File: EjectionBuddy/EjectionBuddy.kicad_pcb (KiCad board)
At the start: 4 copper layers, 48 x 53.5 mm, 117 parts, among them J10 Conn_01x04, J11 Conn_01x02, J12 Conn_01x04, J13 Conn_01x04, J14 Conn_01x08, J15 USB_C_Receptacle_USB2.0_14P, J2 Conn_01x04, J3 Conn_01x04, J4 Conn_01x04, J5 Conn_01x04, J6 Conn_01x08, J7 Conn_01x04, J8 Conn_01x04, J9 Conn_01x04, Q1 NCE55P04S, Q2 NCE55P04S, Q3 UMH3N, Q4 UMH3N, Q5 UMH3N, SW1 SW_Push, SW2 SW_Push, SW3 SW_Push, U1 INA186xxQDCK, U10 TLP291, U11 ESP32-S3-MINI-1, U12 BMP280, U13 EjectionBuddyStamp, U2 GenericBuck_5V, U3 ME6203A50PG, U4 LP5912-3.3DRV, U5 LM66200DRLR, U6 LP5912-3.3DRV, U7 STM32G031K8Ux, U8 MPU-6050, U9 TLP291

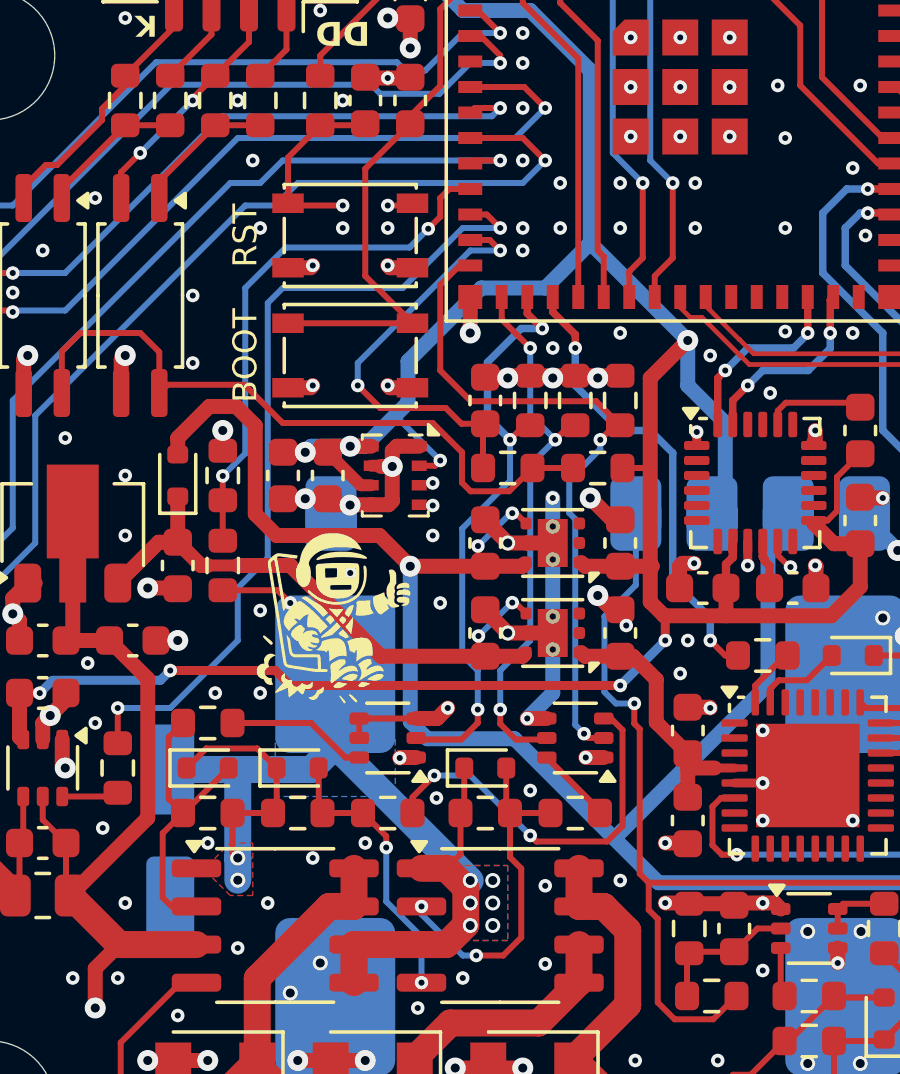
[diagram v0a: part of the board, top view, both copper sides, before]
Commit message: Slight improvements on routing and schematic
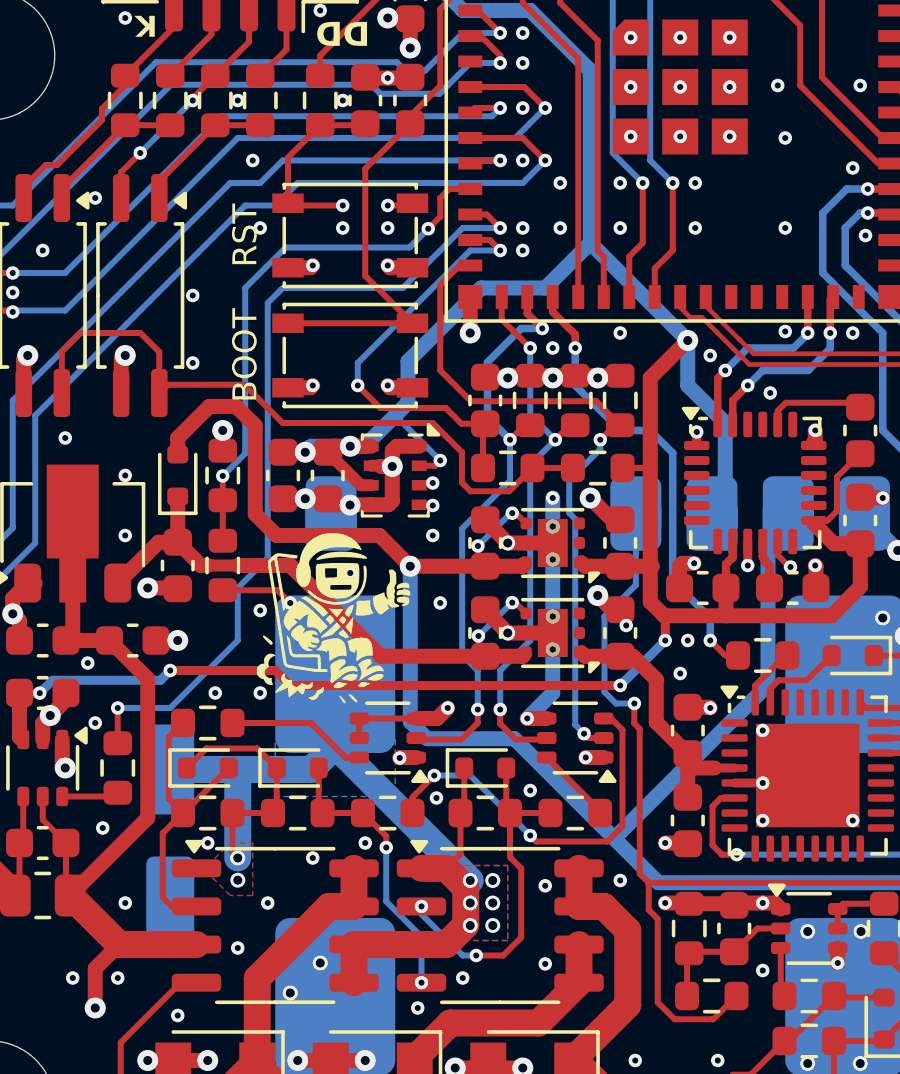
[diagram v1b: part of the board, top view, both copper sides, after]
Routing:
- net /main_mcu/EN: track 35.8 -> 34.3 mm

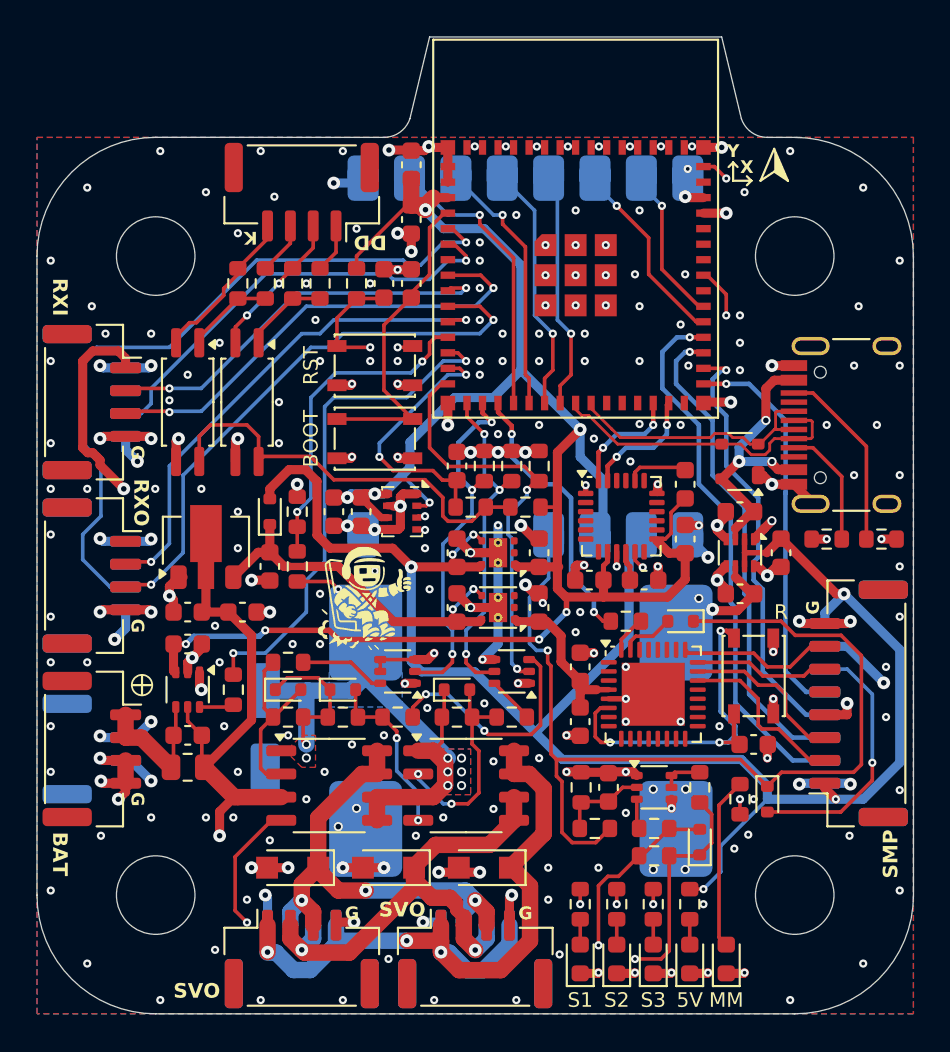
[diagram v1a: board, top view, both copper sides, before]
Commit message: Side-mcu stm -> attiny, with improvements here and there
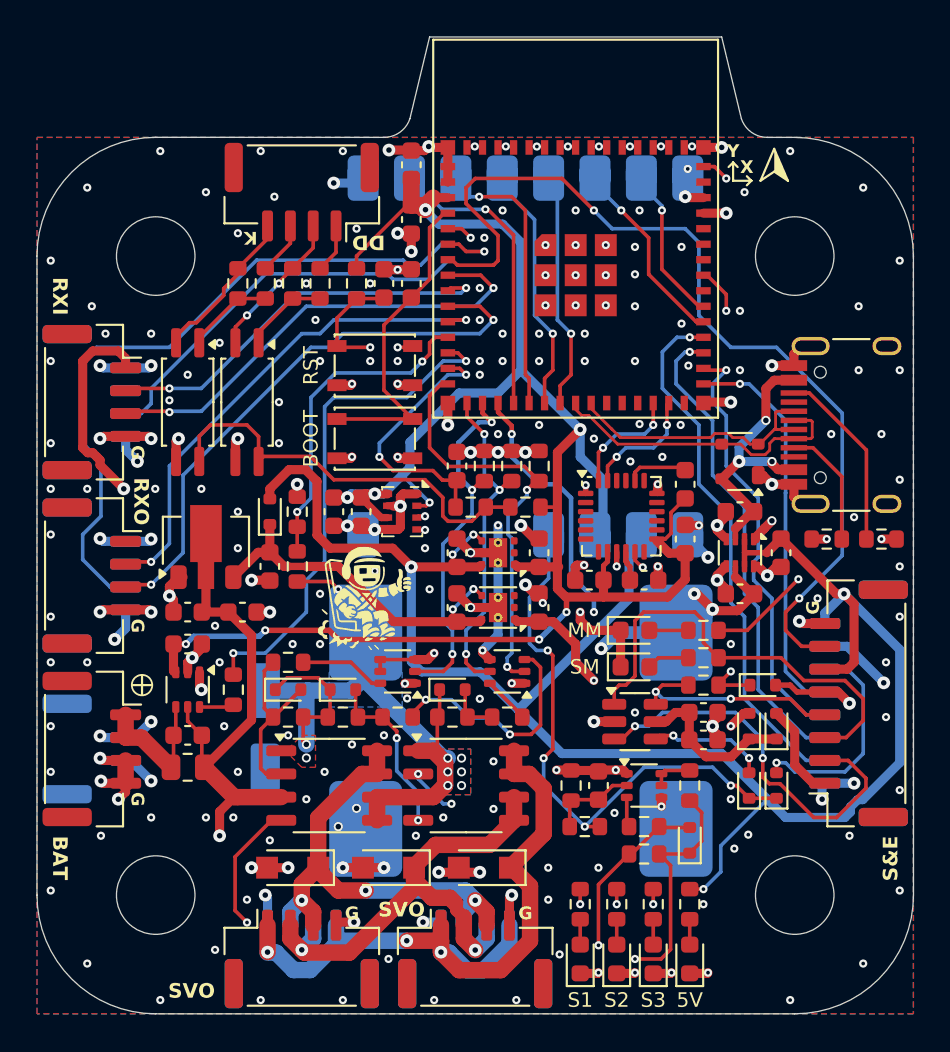
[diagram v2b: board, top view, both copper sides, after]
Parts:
- removed the C17 at (182.8, 106.8)
- removed the J14 at (188.5, 104.5)
- removed the SW1 at (182.8, 103.0)
- added D12: D_Schottky, Diode_SMD:D_SOD-523, F.Cu at (182.5, 105.8)
- added D13: D_Schottky, Diode_SMD:D_SOD-523, F.Cu at (182.5, 109.0)
- added D14: D_Zener, Diode_SMD:D_SOD-523, F.Cu at (183.2, 103.5)
- added D15: LED, LED_SMD:LED_0603_1608Metric, F.Cu at (176.2, 102.5)
- added J13: Conn_01x08, Connector_JST:JST_GH_SM08B-GHS-TB_1x08-1MP_P1.25mm_Horizontal, F.Cu at (188.5, 104.5)
- added R22: 1k, Resistor_SMD:R_0603_1608Metric, F.Cu at (180.0, 102.0)
- R2: renamed from R1; value 0.015 -> 0.05
- U7: value STM32G031K8Ux -> ATtiny10-TS; footprint Package_DFN_QFN:QFN-32-1EP_5x5mm_P0.5mm_EP3.45x3.45mm -> Package_TO_SOT_SMD:SOT-23-6
- moved D16 18.7 mm to (176.2, 100.5), turned to 0 degrees
- moved R23 9.46 mm to (180.0, 100.5), turned to 180 degrees
- moved C15 7.85 mm to (180.0, 106.5), turned to 0 degrees
- moved D11 7.79 mm to (184.0, 105.8), turned to 90 degrees
- moved C16 6.77 mm to (180.0, 105.0), turned to 0 degrees
- moved R21 5.51 mm to (180.0, 103.5), turned to 0 degrees
- moved U7 1.80 mm to (176.2, 105.5)
- moved D9 0.90 mm to (184.0, 109.0), turned to 90 degrees
- moved C14 0.56 mm to (174.2, 109.0)
- moved D8 0.56 mm to (179.2, 112.0)
- moved Q5 0.56 mm to (176.8, 109.0)
- moved R14 0.56 mm to (176.8, 112.8)
- moved R15 0.56 mm to (179.2, 109.0)
- moved R16 0.56 mm to (176.8, 111.2)
- moved R17 0.56 mm to (173.5, 111.2)
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- renumbered C18 to C17, C19 to C18, C20 to C19, C21 to C20, C22 to C21, C23 to C22, C24 to C23, C25 to C24, C26 to C25, C36 to C26, C37 to C27, D12 to D16, D13 to D17, D14 to D18, D15 to D19, D16 to D20, J2 to J1, J11 to J10, J12 to J11, J13 to J12, J15 to J14, J3 to J2, J4 to J3, J5 to J4, J6 to J5, J7 to J6, J8 to J7, J9 to J8, J10 to J9, R3 to R1, R22 to R23, R23 to R24, R24 to R25, R25 to R26, R26 to R27, R27 to R28, R28 to R29, R2 to R3, R29 to R30, R30 to R31, R31 to R32, R32 to R33, R33 to R34, SW2 to SW1, SW3 to SW2
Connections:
- C15 pad 1: +3.3S -> Net-(D11-K)
- C16 pad 1: +3.3S -> Net-(D11-K)
- D11 pad 1: /SW_PWRCUT -> Net-(D11-K)
- D11 pad 2: Net-(D11-A) -> +5S
- R21 pad 1: Net-(U7-PB8) -> /SM.RESET
- U11 pad 7: unconnected-(U11-IO3-Pad7) -> /MM.GPIO3
- U7 pad 1: unconnected-(U7-PB9-Pad1) -> /SM.TPIDATA
- U7 pad 2: unconnected-(U7-PC14-Pad2) -> GND
- U7 pad 3: unconnected-(U7-PC15-Pad3) -> /SM.TPICLK
- U7 pad 4: +3.3S -> Net-(D13-A)
- U7 pad 5: GND -> Net-(D11-K)
- U7 pad 6: /side_mcu/RST -> /SM.RESET
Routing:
- net /MM.GPIO3: track 0.00 -> 51.9 mm, vias 0 -> 2
- net /side_mcu/RST: track 27.1 -> 0.00 mm, vias 3 -> 0
- net /SM.TPIDATA: track 0.00 -> 24.6 mm
- net /SW_PWRCUT: track 54.4 -> 31.4 mm, vias 1 -> 4
- net /SM.TPICLK: track 0.00 -> 21.8 mm, vias 0 -> 2
- net /MM.GPIO14: track 15.3 -> 30.1 mm, vias 2 -> 3
- net /SM.RESET: track 0.00 -> 12.4 mm, vias 0 -> 2
- net /MM.GPIO42: track 38.7 -> 27.7 mm
- net /SM.TX: track 9.63 -> 0.00 mm
- net Net-(D11-K): track 0.00 -> 9.11 mm
- net /SM.RX: track 9.09 -> 0.00 mm
- net /SM.CLK: track 8.50 -> 0.00 mm
- net +3.3S: track 8.79 -> 16.3 mm, vias 0 -> 2
- net /SM.DIO: track 7.43 -> 0.00 mm
- net Net-(D16-A): track 9.43 -> 2.14 mm
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- removed copper zone on In2.Cu, net +5V
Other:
- board text added: "E2"
- board text added: "S&E"
- board text added: "SM"
- board text removed: "EXT"
- board text removed: "R"
- board text removed: "SMP"

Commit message: Prodection version hw1.0 finished, with tidy-ups and bug-fixes
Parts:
- added G***: LOGO, LOGO, B.Cu at (154.5, 91.5)
- D14: value D_Zener -> D_Zener3V6
- D15, D16: value LED -> LED_G
- D17, D18, D19, D20: value LED -> LED_R
- D2, D3, D4, D8: value D_Zener -> D_Zener7V5
- U1: value INA186xxQDCK -> INA186A1
- renumbered J11 to J10, J12 to J11, J13 to J12, J5 to J13, J6 to J5, J7 to J6, J8 to J7, J9 to J8, J10 to J9
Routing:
- net Net-(D2-A): track 5.56 -> 11.8 mm
- net /MM.GPIO1: track 38.8 -> 40.4 mm
- net /MM.GPIO2: track 24.0 -> 24.7 mm
- net GND: track 139.2 -> 138.9 mm, vias 247 -> 253
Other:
- board text added: "#EjectionBuddy"

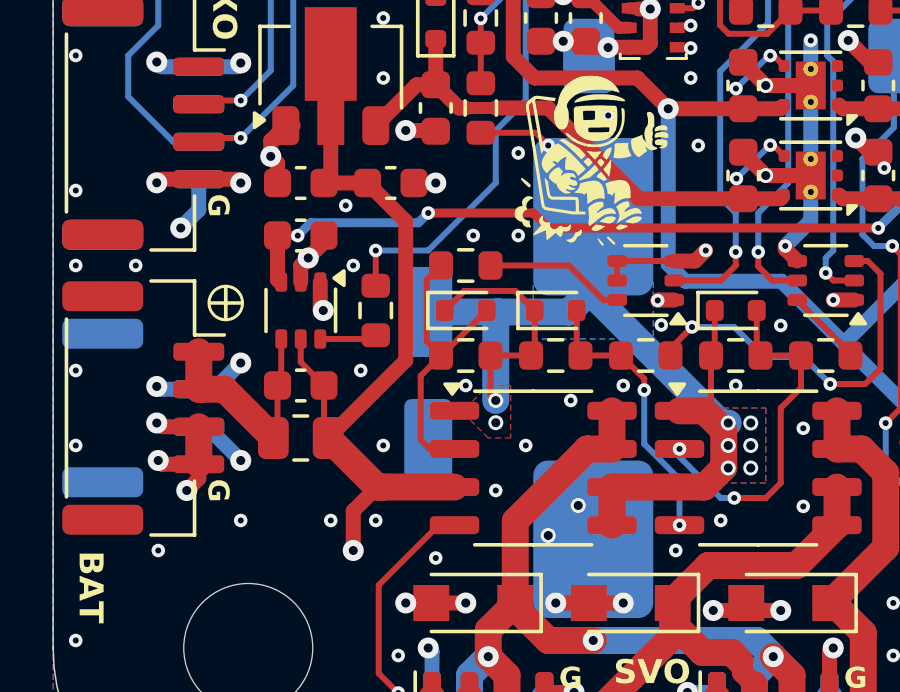
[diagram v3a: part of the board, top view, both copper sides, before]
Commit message: Fix the e-cap footprint, we'll keep the 1.0
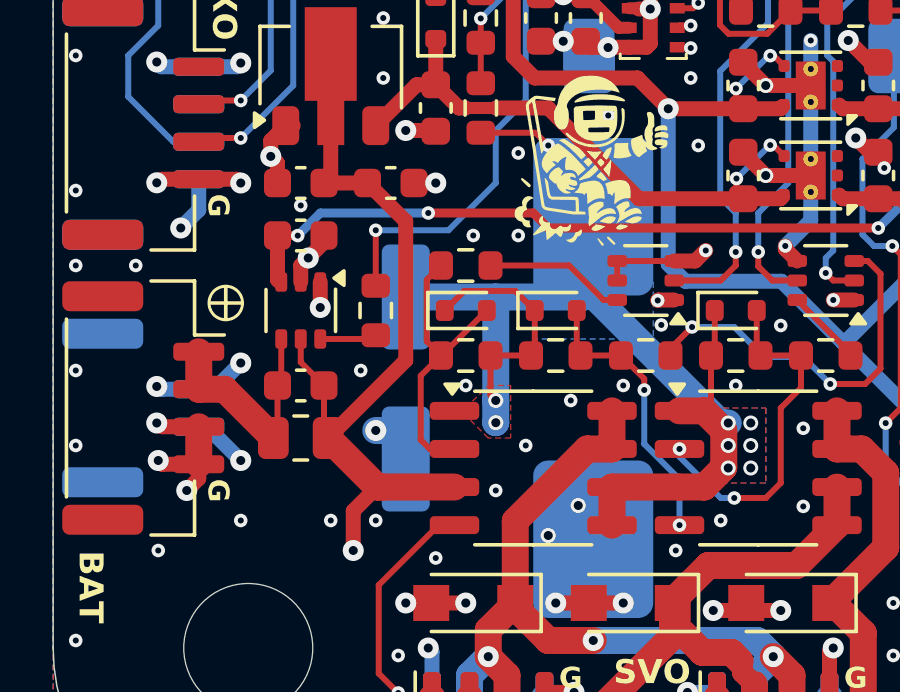
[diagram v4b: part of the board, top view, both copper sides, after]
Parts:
- C3: footprint Capacitor_SMD:CP_Elec_5x4.5 -> Capacitor_SMD:CP_Elec_6.3x5.8
- moved C3 0.75 mm to (155.2, 106.0)
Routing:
- net GND: track 138.9 -> 140.0 mm, vias 253 -> 252
- net VM: track 52.7 -> 53.7 mm

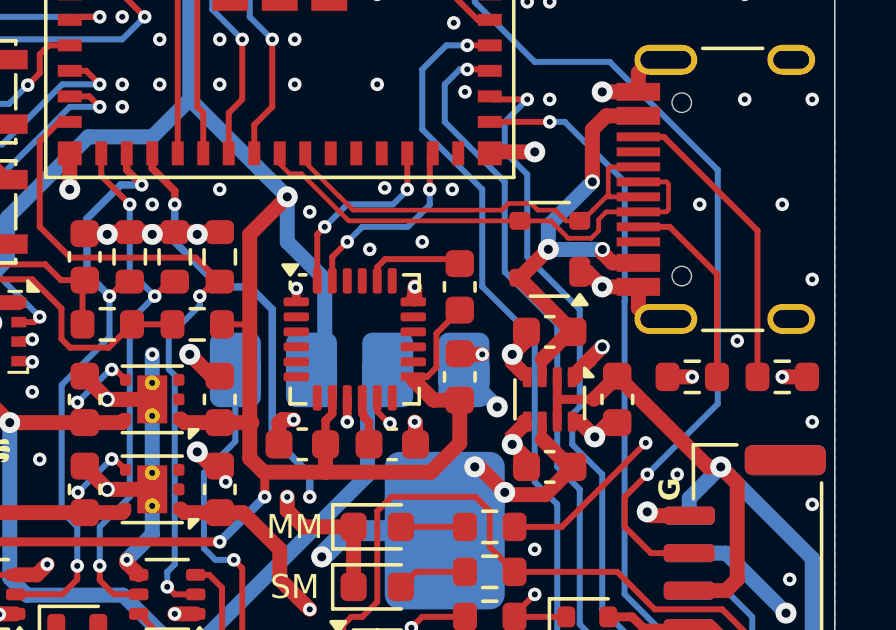
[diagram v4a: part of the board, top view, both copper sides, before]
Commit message: Fixed a FATAL imu wiring fault, CPOUT
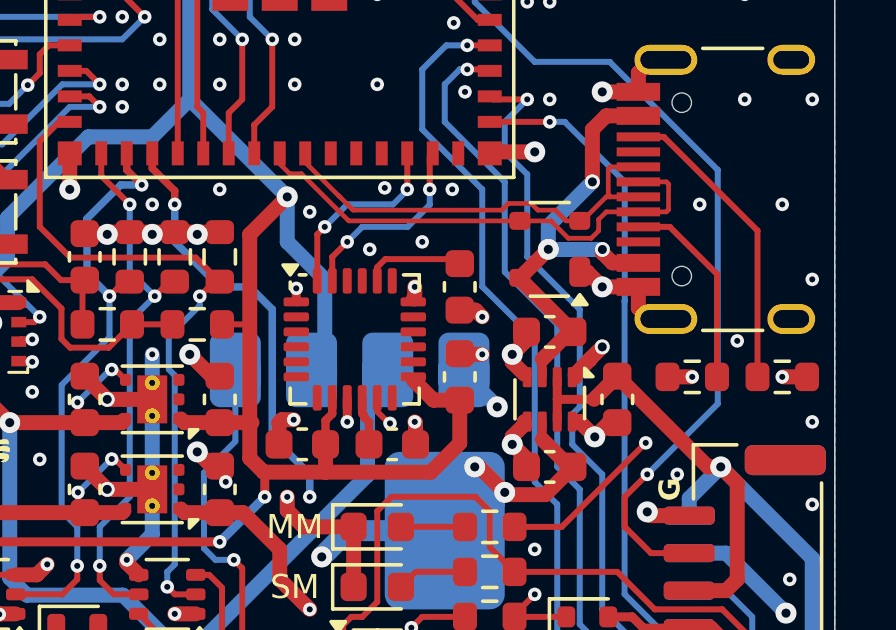
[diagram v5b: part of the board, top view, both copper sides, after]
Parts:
- turned C19 to -90 degrees
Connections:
- C19 pad 1: +3.3V -> Net-(U8-CPOUT)
- C19 pad 2: Net-(U8-CPOUT) -> GND
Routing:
- net +3.3V: track 107.9 -> 104.8 mm
- net GND: track 140.0 -> 140.8 mm, vias 252 -> 253
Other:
- board text added: "HW1.1 TZ-2025"
- board text removed: "HW1.0 TZ-2025"
